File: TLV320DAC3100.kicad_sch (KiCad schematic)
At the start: 2 parts, among them U3 TLV320DAC3100IRHBR

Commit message: updated board design
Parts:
- U3: footprint TLV320DAC3100IRHBR:IC_ADS125H01IRHBT -> TLV320DAC3100:IC_ADS125H01IRHBT
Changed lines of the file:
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@@
 			)
 		)
-		(property "Footprint" "TLV320DAC3100IRHBR:IC_ADS125H01IRHBT"
+		(property "Footprint" "TLV320DAC3100:IC_ADS125H01IRHBT"
 			(at 129.54 82.55 0)
 			(hide yes)

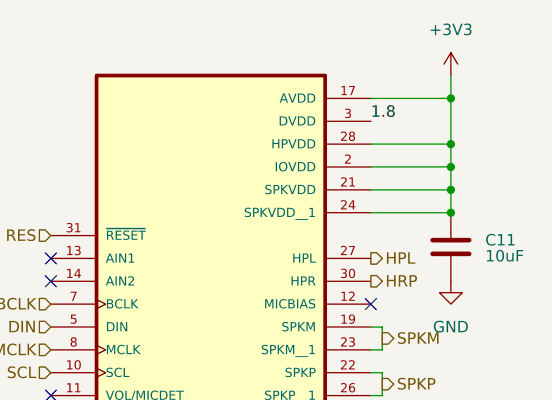
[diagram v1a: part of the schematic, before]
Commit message: updated board design to fit altoid tin
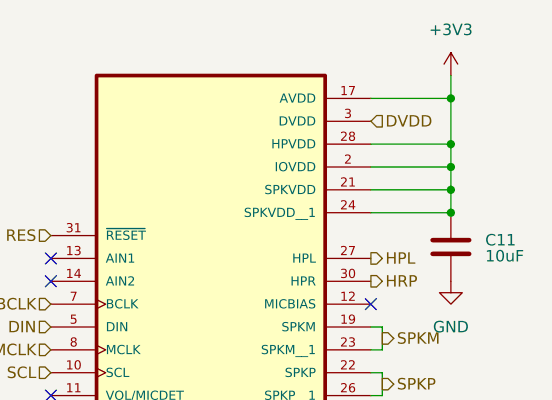
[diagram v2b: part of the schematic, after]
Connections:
- net 1.8 renamed DVDD
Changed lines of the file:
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@@
-		)
-	)
-	(label "1.8"
-		(at 147.32 52.07 0)
-		(effects
-			(font
-				(size 1.27 1.27)
-			)
-			(justify left bottom)
 		)
 	)
@@
 		)
 	)
+	(hierarchical_label "DVDD"
+		(shape input)
+		(at 147.32 52.07 0)
+		(effects
+			(font
+				(size 1.27 1.27)
+			)
+			(justify left)
+		)
+	)
